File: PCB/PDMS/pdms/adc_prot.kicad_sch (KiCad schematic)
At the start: 28 parts

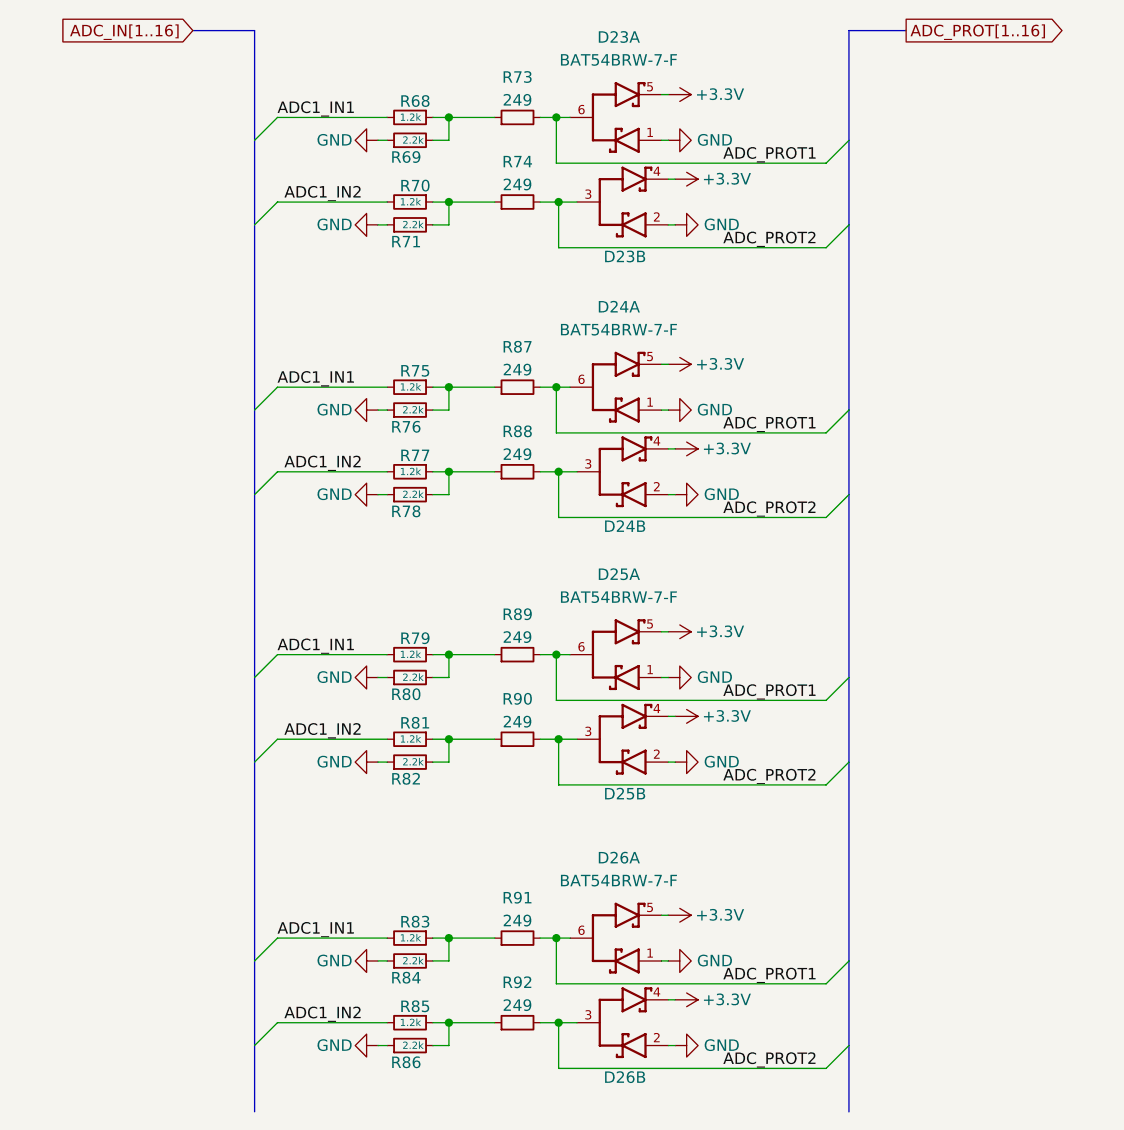
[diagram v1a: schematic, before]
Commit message: Changed MCU to L496 & finished powerswitch section
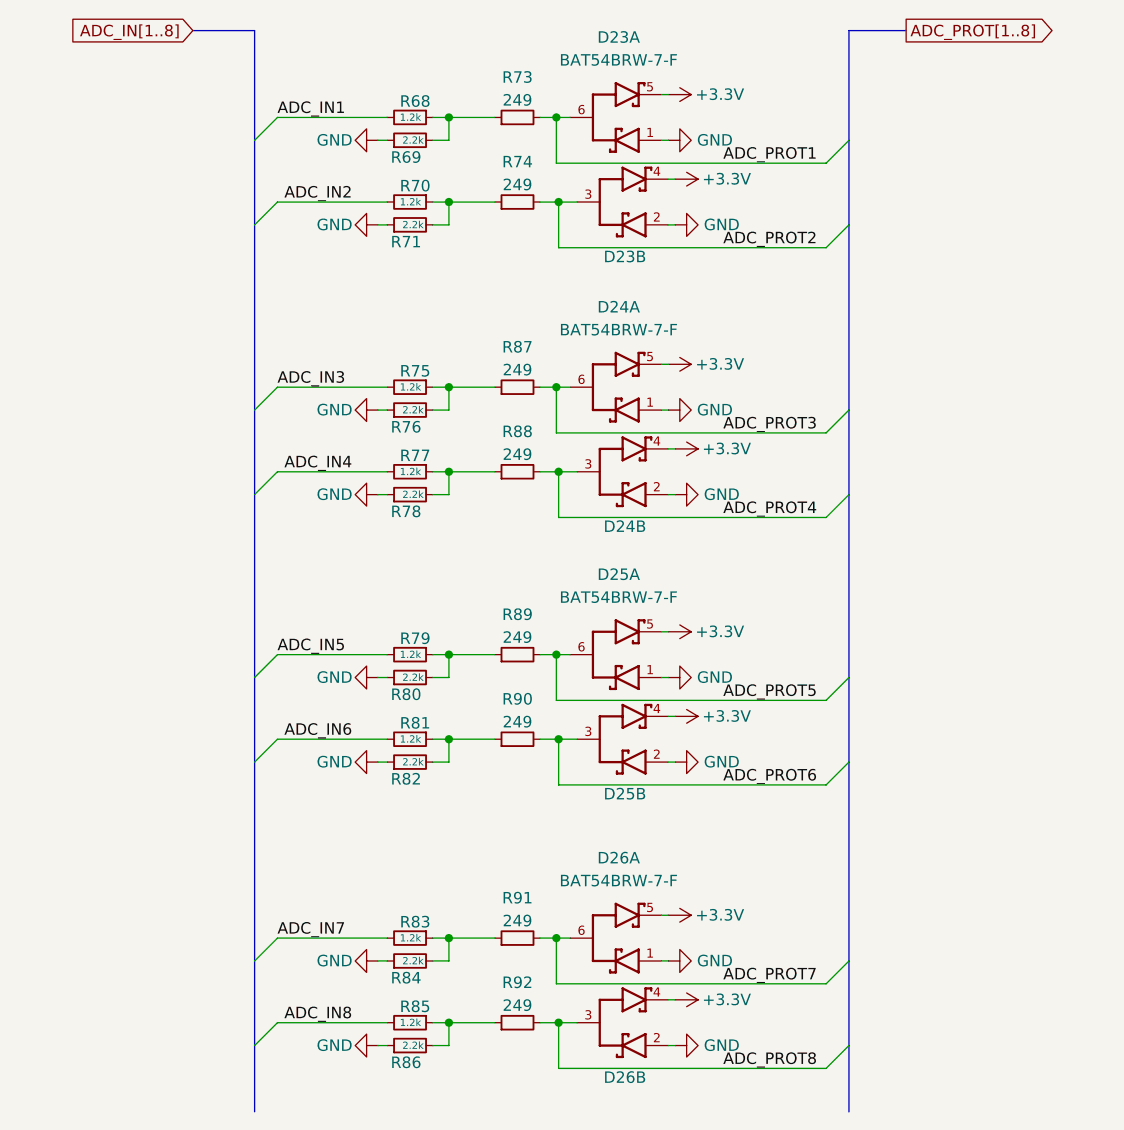
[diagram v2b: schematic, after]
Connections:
- net ADC_PROT1: no longer D24.6, D25.6, D26.6, R87.2, R89.2, R91.2
- net ADC_PROT2: no longer D24.3, D25.3, D26.3, R88.2, R90.2, R92.2
- removed net ADC1_IN1: R68.2, R75.2, R79.2, R83.2
- removed net ADC1_IN2: R70.2, R77.2, R81.2, R85.2
- new net ADC_IN1: R68.2
- new net ADC_IN2: R70.2
- new net ADC_IN3: R75.2
- new net ADC_IN4: R77.2
- new net ADC_IN5: R79.2
- new net ADC_IN6: R81.2
- new net ADC_IN7: R83.2
- new net ADC_IN8: R85.2
- new net ADC_PROT3: D24.6, R87.2
- new net ADC_PROT4: D24.3, R88.2
- new net ADC_PROT5: D25.6, R89.2
- new net ADC_PROT6: D25.3, R90.2
- new net ADC_PROT7: D26.6, R91.2
- new net ADC_PROT8: D26.3, R92.2
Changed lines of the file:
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@@
     (stroke (width 0) (type default) (color 0 0 0 0))
   )
-  (label "ADC1_IN1" (at 59.69 140.208 0)
+  (label "ADC_IN7" (at 59.69 140.208 0)
     (effects (font (size 1.27 1.27)) (justify left bottom))
   )
-  (label "ADC_PROT2" (at 109.22 93.472 0)
+  (label "ADC_PROT4" (at 109.22 93.472 0)
     (effects (font (size 1.27 1.27)) (justify left bottom))
   )
@@
     (effects (font (size 1.27 1.27)) (justify left bottom))
   )
-  (label "ADC1_IN1" (at 59.69 49.022 0)
+  (label "ADC_IN1" (at 59.69 49.022 0)
     (effects (font (size 1.27 1.27)) (justify left bottom))
   )
-  (label "ADC1_IN1" (at 59.69 108.712 0)
+  (label "ADC_IN5" (at 59.69 108.712 0)
     (effects (font (size 1.27 1.27)) (justify left bottom))
   )
-  (label "ADC1_IN2" (at 60.452 149.606 0)
+  (label "ADC_IN8" (at 60.452 149.606 0)
     (effects (font (size 1.27 1.27)) (justify left bottom))
   )
-  (label "ADC_PROT2" (at 109.22 123.19 0)
+  (label "ADC_PROT6" (at 109.22 123.19 0)
     (effects (font (size 1.27 1.27)) (justify left bottom))
   )
-  (label "ADC_PROT1" (at 109.22 113.792 0)
+  (label "ADC_PROT5" (at 109.22 113.792 0)
     (effects (font (size 1.27 1.27)) (justify left bottom))
   )
-  (label "ADC1_IN1" (at 59.69 78.994 0)
+  (label "ADC_IN3" (at 59.69 78.994 0)
     (effects (font (size 1.27 1.27)) (justify left bottom))
   )
-  (label "ADC_PROT1" (at 109.22 145.288 0)
+  (label "ADC_PROT7" (at 109.22 145.288 0)
     (effects (font (size 1.27 1.27)) (justify left bottom))
   )
-  (label "ADC1_IN2" (at 60.452 88.392 0)
+  (label "ADC_IN4" (at 60.452 88.392 0)
     (effects (font (size 1.27 1.27)) (justify left bottom))
   )
@@
     (effects (font (size 1.27 1.27)) (justify left bottom))
   )
-  (label "ADC_PROT1" (at 109.22 84.074 0)
+  (label "ADC_PROT3" (at 109.22 84.074 0)
     (effects (font (size 1.27 1.27)) (justify left bottom))
   )
-  (label "ADC1_IN2" (at 60.452 118.11 0)
+  (label "ADC_IN6" (at 60.452 118.11 0)
     (effects (font (size 1.27 1.27)) (justify left bottom))
   )
-  (label "ADC1_IN2" (at 60.452 58.42 0)
+  (label "ADC_IN2" (at 60.452 58.42 0)
     (effects (font (size 1.27 1.27)) (justify left bottom))
   )
-  (label "ADC_PROT2" (at 109.22 154.686 0)
+  (label "ADC_PROT8" (at 109.22 154.686 0)
     (effects (font (size 1.27 1.27)) (justify left bottom))
   )
-  (global_label "ADC_IN[1..16]" (shape input) (at 50.292 39.37 180) (fields_autoplaced)
+  (global_label "ADC_IN[1..8]" (shape input) (at 50.292 39.37 180) (fields_autoplaced)
     (effects (font (size 1.27 1.27)) (justify right))
-    (property "Intersheet References" "${INTERSHEET_REFS}" (id 0) (at 34.816 39.2906 0)
+    (property "Intersheet References" "${INTERSHEET_REFS}" (id 0) (at 36.0256 39.2906 0)
       (effects (font (size 1.27 1.27)) (justify right) hide)
     )
   )
-  (global_label "ADC_PROT[1..16]" (shape output) (at 129.54 39.37 0) (fields_autoplaced)
+  (global_label "ADC_PROT[1..8]" (shape output) (at 129.54 39.37 0) (fields_autoplaced)
     (effects (font (size 1.27 1.27)) (justify left))
-    (property "Intersheet References" "${INTERSHEET_REFS}" (id 0) (at 147.9188 39.4494 0)
+    (property "Intersheet References" "${INTERSHEET_REFS}" (id 0) (at 146.7093 39.2906 0)
       (effects (font (size 1.27 1.27)) (justify left) hide)
     )

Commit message: Added connector and more
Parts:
- R68, R69, R70, R71, R73, R74, R75, R76, R77, R78, R79, R80, R81, R82, R83, R84, R85, R86, R87, R88, R89, R90, R91, R92: footprint Resistor_SMD:R_0402_1005Metric_Pad0.72x0.64mm_HandSolder -> Resistor_SMD:R_0402_1005Metric
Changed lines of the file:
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@@
     (property "Reference" "R87" (id 0) (at 86.36 74.549 90))
     (property "Value" "249" (id 1) (at 86.36 77.089 90))
-    (property "Footprint" "Resistor_SMD:R_0402_1005Metric_Pad0.72x0.64mm_HandSolder" (id 2) (at 86.36 78.994 0)
+    (property "Footprint" "Resistor_SMD:R_0402_1005Metric" (id 2) (at 86.36 78.994 0)
       (effects (font (size 1.27 1.27)) hide)
     )
@@
       (effects (font (size 0.8 0.8)) (justify left))
     )
-    (property "Footprint" "Resistor_SMD:R_0402_1005Metric_Pad0.72x0.64mm_HandSolder" (id 2) (at 74.422 78.994 0)
+    (property "Footprint" "Resistor_SMD:R_0402_1005Metric" (id 2) (at 74.422 78.994 0)
       (effects (font (size 1.27 1.27)) hide)
     )
@@
     (property "Reference" "R89" (id 0) (at 86.36 104.267 90))
     (property "Value" "249" (id 1) (at 86.36 106.807 90))
-    (property "Footprint" "Resistor_SMD:R_0402_1005Metric_Pad0.72x0.64mm_HandSolder" (id 2) (at 86.36 108.712 0)
+    (property "Footprint" "Resistor_SMD:R_0402_1005Metric" (id 2) (at 86.36 108.712 0)
       (effects (font (size 1.27 1.27)) hide)
     )
@@
     (property "Reference" "R88" (id 0) (at 86.36 83.947 90))
     (property "Value" "249" (id 1) (at 86.36 86.487 90))
-    (property "Footprint" "Resistor_SMD:R_0402_1005Metric_Pad0.72x0.64mm_HandSolder" (id 2) (at 86.36 88.392 0)
+    (property "Footprint" "Resistor_SMD:R_0402_1005Metric" (id 2) (at 86.36 88.392 0)
       (effects (font (size 1.27 1.27)) hide)
     )
@@
     (property "Reference" "R90" (id 0) (at 86.36 113.665 90))
     (property "Value" "249" (id 1) (at 86.36 116.205 90))
-    (property "Footprint" "Resistor_SMD:R_0402_1005Metric_Pad0.72x0.64mm_HandSolder" (id 2) (at 86.36 118.11 0)
+    (property "Footprint" "Resistor_SMD:R_0402_1005Metric" (id 2) (at 86.36 118.11 0)
       (effects (font (size 1.27 1.27)) hide)
     )
@@
       (effects (font (size 0.8 0.8)) (justify left))
     )
-    (property "Footprint" "Resistor_SMD:R_0402_1005Metric_Pad0.72x0.64mm_HandSolder" (id 2) (at 74.422 111.252 0)
+    (property "Footprint" "Resistor_SMD:R_0402_1005Metric" (id 2) (at 74.422 111.252 0)
       (effects (font (size 1.27 1.27)) hide)
     )
@@
       (effects (font (size 0.8 0.8)) (justify left))
     )
-    (property "Footprint" "Resistor_SMD:R_0402_1005Metric_Pad0.72x0.64mm_HandSolder" (id 2) (at 74.422 108.712 0)
+    (property "Footprint" "Resistor_SMD:R_0402_1005Metric" (id 2) (at 74.422 108.712 0)
       (effects (font (size 1.27 1.27)) hide)
     )
@@
       (effects (font (size 0.8 0.8)) (justify left))
     )
-    (property "Footprint" "Resistor_SMD:R_0402_1005Metric_Pad0.72x0.64mm_HandSolder" (id 2) (at 74.422 81.534 0)
+    (property "Footprint" "Resistor_SMD:R_0402_1005Metric" (id 2) (at 74.422 81.534 0)
       (effects (font (size 1.27 1.27)) hide)
     )
@@
       (effects (font (size 0.8 0.8)) (justify left))
     )
-    (property "Footprint" "Resistor_SMD:R_0402_1005Metric_Pad0.72x0.64mm_HandSolder" (id 2) (at 74.422 120.65 0)
+    (property "Footprint" "Resistor_SMD:R_0402_1005Metric" (id 2) (at 74.422 120.65 0)
       (effects (font (size 1.27 1.27)) hide)
     )
@@
       (effects (font (size 0.8 0.8)) (justify left))
     )
-    (property "Footprint" "Resistor_SMD:R_0402_1005Metric_Pad0.72x0.64mm_HandSolder" (id 2) (at 74.422 58.42 0)
+    (property "Footprint" "Resistor_SMD:R_0402_1005Metric" (id 2) (at 74.422 58.42 0)
       (effects (font (size 1.27 1.27)) hide)
     )
@@
       (effects (font (size 0.8 0.8)) (justify left))
     )
-    (property "Footprint" "Resistor_SMD:R_0402_1005Metric_Pad0.72x0.64mm_HandSolder" (id 2) (at 74.422 140.208 0)
+    (property "Footprint" "Resistor_SMD:R_0402_1005Metric" (id 2) (at 74.422 140.208 0)
       (effects (font (size 1.27 1.27)) hide)
     )
@@
     (property "Reference" "R91" (id 0) (at 86.36 135.763 90))
     (property "Value" "249" (id 1) (at 86.36 138.303 90))
-    (property "Footprint" "Resistor_SMD:R_0402_1005Metric_Pad0.72x0.64mm_HandSolder" (id 2) (at 86.36 140.208 0)
+    (property "Footprint" "Resistor_SMD:R_0402_1005Metric" (id 2) (at 86.36 140.208 0)
       (effects (font (size 1.27 1.27)) hide)
     )
@@
       (effects (font (size 0.8 0.8)) (justify left))
     )
-    (property "Footprint" "Resistor_SMD:R_0402_1005Metric_Pad0.72x0.64mm_HandSolder" (id 2) (at 74.422 118.11 0)
+    (property "Footprint" "Resistor_SMD:R_0402_1005Metric" (id 2) (at 74.422 118.11 0)
       (effects (font (size 1.27 1.27)) hide)
     )
@@
       (effects (font (size 0.8 0.8)) (justify left))
     )
-    (property "Footprint" "Resistor_SMD:R_0402_1005Metric_Pad0.72x0.64mm_HandSolder" (id 2) (at 74.422 152.146 0)
+    (property "Footprint" "Resistor_SMD:R_0402_1005Metric" (id 2) (at 74.422 152.146 0)
       (effects (font (size 1.27 1.27)) hide)
     )
@@
       (effects (font (size 0.8 0.8)) (justify left))
     )
-    (property "Footprint" "Resistor_SMD:R_0402_1005Metric_Pad0.72x0.64mm_HandSolder" (id 2) (at 74.422 88.392 0)
+    (property "Footprint" "Resistor_SMD:R_0402_1005Metric" (id 2) (at 74.422 88.392 0)
       (effects (font (size 1.27 1.27)) hide)
     )
@@
     (property "Reference" "R74" (id 0) (at 86.36 53.975 90))
     (property "Value" "249" (id 1) (at 86.36 56.515 90))
-    (property "Footprint" "Resistor_SMD:R_0402_1005Metric_Pad0.72x0.64mm_HandSolder" (id 2) (at 86.36 58.42 0)
+    (property "Footprint" "Resistor_SMD:R_0402_1005Metric" (id 2) (at 86.36 58.42 0)
       (effects (font (size 1.27 1.27)) hide)
     )
@@
       (effects (font (size 0.8 0.8)) (justify left))
     )
-    (property "Footprint" "Resistor_SMD:R_0402_1005Metric_Pad0.72x0.64mm_HandSolder" (id 2) (at 74.422 142.748 0)
+    (property "Footprint" "Resistor_SMD:R_0402_1005Metric" (id 2) (at 74.422 142.748 0)
       (effects (font (size 1.27 1.27)) hide)
     )
@@
       (effects (font (size 0.8 0.8)) (justify left))
     )
-    (property "Footprint" "Resistor_SMD:R_0402_1005Metric_Pad0.72x0.64mm_HandSolder" (id 2) (at 74.422 60.96 0)
+    (property "Footprint" "Resistor_SMD:R_0402_1005Metric" (id 2) (at 74.422 60.96 0)
       (effects (font (size 1.27 1.27)) hide)
     )
@@
       (effects (font (size 0.8 0.8)) (justify left))
     )
-    (property "Footprint" "Resistor_SMD:R_0402_1005Metric_Pad0.72x0.64mm_HandSolder" (id 2) (at 74.422 49.022 0)
+    (property "Footprint" "Resistor_SMD:R_0402_1005Metric" (id 2) (at 74.422 49.022 0)
       (effects (font (size 1.27 1.27)) hide)
     )
@@
     (property "Reference" "R73" (id 0) (at 86.36 44.577 90))
     (property "Value" "249" (id 1) (at 86.36 47.117 90))
-    (property "Footprint" "Resistor_SMD:R_0402_1005Metric_Pad0.72x0.64mm_HandSolder" (id 2) (at 86.36 49.022 0)
+    (property "Footprint" "Resistor_SMD:R_0402_1005Metric" (id 2) (at 86.36 49.022 0)
       (effects (font (size 1.27 1.27)) hide)
     )
@@
     (property "Reference" "R92" (id 0) (at 86.36 145.161 90))
     (property "Value" "249" (id 1) (at 86.36 147.701 90))
-    (property "Footprint" "Resistor_SMD:R_0402_1005Metric_Pad0.72x0.64mm_HandSolder" (id 2) (at 86.36 149.606 0)
+    (property "Footprint" "Resistor_SMD:R_0402_1005Metric" (id 2) (at 86.36 149.606 0)
       (effects (font (size 1.27 1.27)) hide)
     )
@@
       (effects (font (size 0.8 0.8)) (justify left))
     )
-    (property "Footprint" "Resistor_SMD:R_0402_1005Metric_Pad0.72x0.64mm_HandSolder" (id 2) (at 74.422 90.932 0)
+    (property "Footprint" "Resistor_SMD:R_0402_1005Metric" (id 2) (at 74.422 90.932 0)
       (effects (font (size 1.27 1.27)) hide)
     )
@@
       (effects (font (size 0.8 0.8)) (justify left))
     )
-    (property "Footprint" "Resistor_SMD:R_0402_1005Metric_Pad0.72x0.64mm_HandSolder" (id 2) (at 74.422 51.562 0)
+    (property "Footprint" "Resistor_SMD:R_0402_1005Metric" (id 2) (at 74.422 51.562 0)
       (effects (font (size 1.27 1.27)) hide)
     )
@@
       (effects (font (size 0.8 0.8)) (justify left))
     )
-    (property "Footprint" "Resistor_SMD:R_0402_1005Metric_Pad0.72x0.64mm_HandSolder" (id 2) (at 74.422 149.606 0)
-      (effects (font (size 1.27 1.27)) hide)
-    )
+    (property "Footprint" "Resistor_SMD:R_0402_1005Metric" (id 2) (at 74.422 149.606 0)
+      (effects (font (size 1.27 1.27)) hide)
+    )

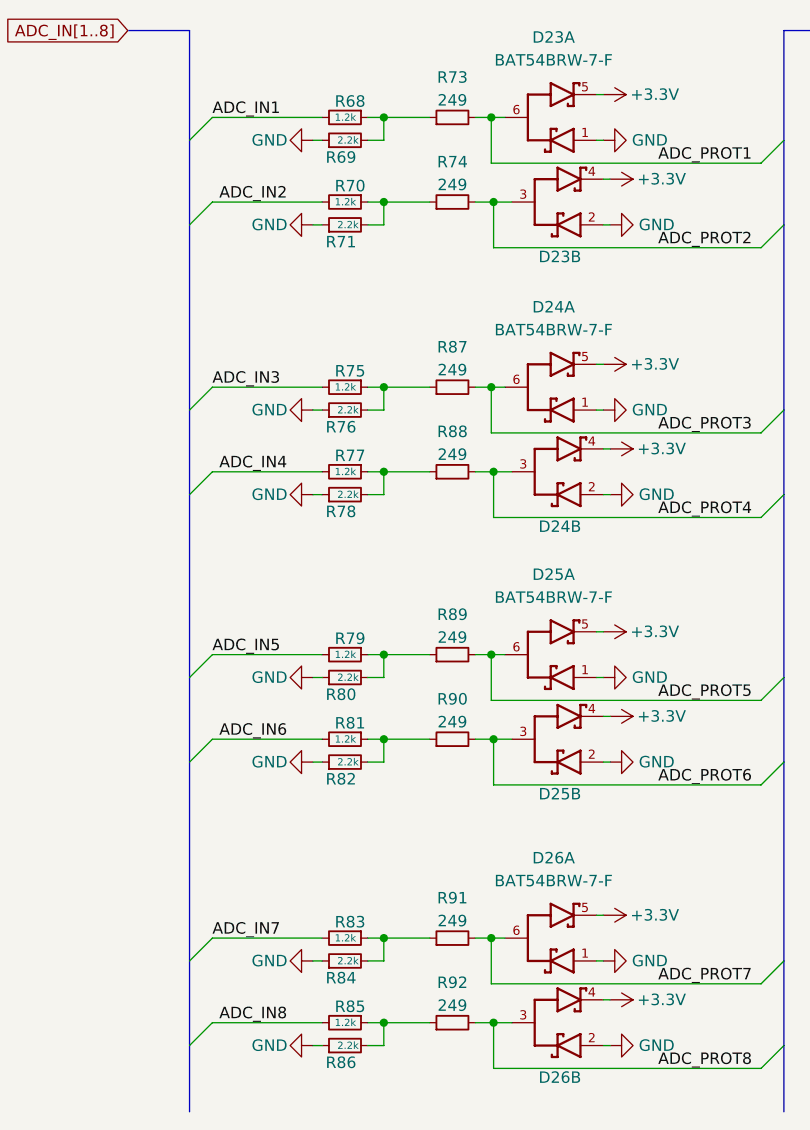
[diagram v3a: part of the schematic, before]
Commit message: ADC protection layout
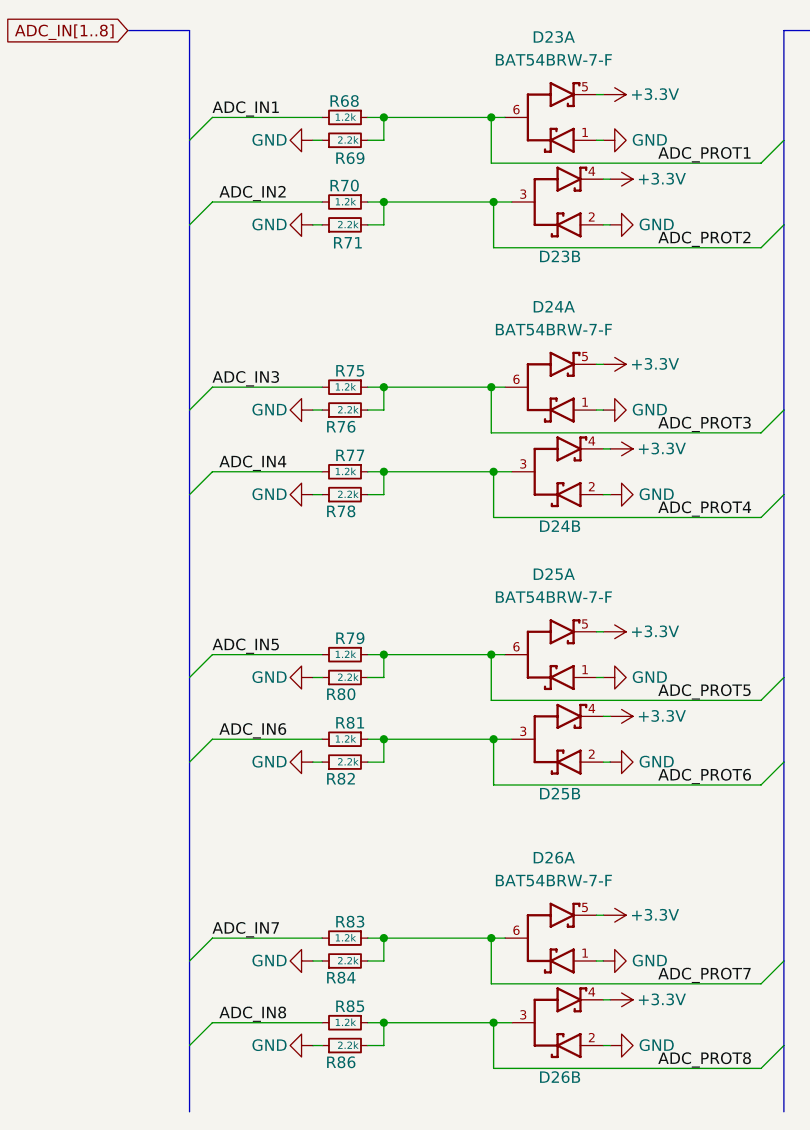
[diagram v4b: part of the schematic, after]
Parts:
- removed R73, R74, R87, R88, R89, R90, R91, R92: 249, Resistor_SMD:R_0402_1005Metric, symbol Device:R_Small
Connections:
- net ADC_PROT1: now also R68.1, R69.2
- net ADC_PROT2: now also R70.1, R71.2
- net ADC_PROT3: now also R75.1, R76.2
- net ADC_PROT4: now also R77.1, R78.2
- net ADC_PROT5: now also R79.1, R80.2
- net ADC_PROT6: now also R81.1, R82.2
- net ADC_PROT7: now also R83.1, R84.2
- net ADC_PROT8: now also R85.1, R86.2

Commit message: Clean-up of schematics
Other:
- note added: "MCU I/O's protection"
- moved on the sheet: D23A, D23B, D24A, D24B, D25A, D25B, D26A, D26B, R68, R69, R70, R71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
